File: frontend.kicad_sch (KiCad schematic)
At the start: 71 parts, among them P3 SMA, Q1 NMOS/PMOS, U12 BGS13SN8, U13 74LVC1G86, U14 BGS13SN8, U24 AP22652, U25 TRF37C73, U40 BGB741L7ESD

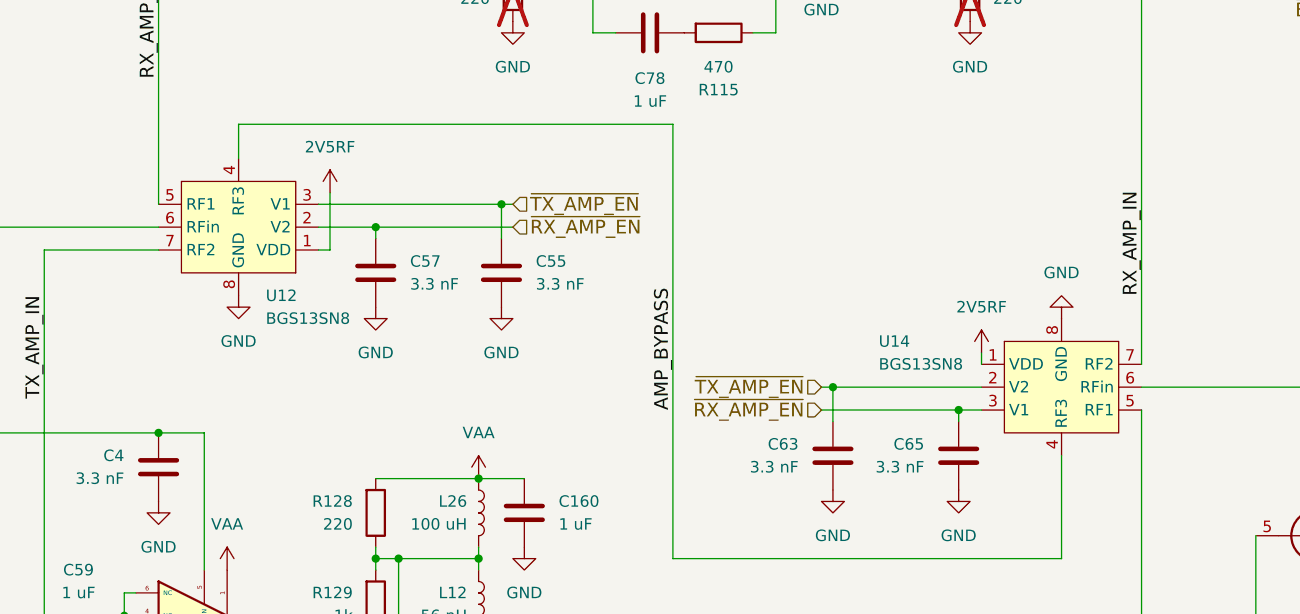
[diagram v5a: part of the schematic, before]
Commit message: Change SP3T RF switches from BGS13SN8 to MXD8638C
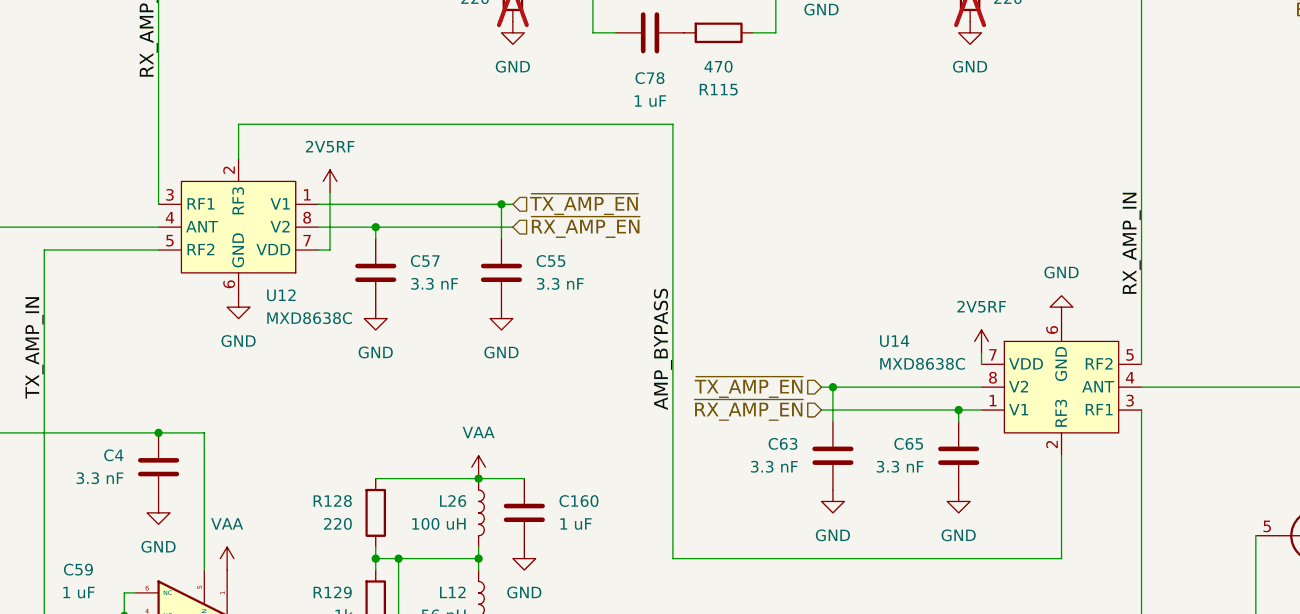
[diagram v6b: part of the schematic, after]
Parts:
- U12, U14: value BGS13SN8 -> MXD8638C; footprint praline:TSNP-9-3 -> praline:MXD8638C; symbol praline:BGS13SN8 -> praline:MXD8638; Manufacturer Infineon -> Maxscend; Part Number BGS13SN8E6327XTSA1 -> MXD8638C
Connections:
- net 2V5RF: now also U12.7 (VDD), U14.7 (VDD); no longer U12.1 (VDD), U14.1 (VDD)
- net AMP_BYPASS: now also U12.2 (RF3), U14.2 (RF3); no longer U12.4 (RF3), U14.4 (RF3)
- net GND: now also U12.6 (GND), U14.6 (GND); no longer U12.8 (GND), U14.8 (GND)
- net RF: now also U12.4 (ANT); no longer U12.6 (RFin)
- net RX_AMP_IN: now also U14.5 (RF2); no longer U14.7 (RF2)
- net RX_AMP_OUT: now also U12.3 (RF1); no longer U12.5 (RF1)
- net TX_AMP_IN: now also U12.5 (RF2); no longer U12.7 (RF2)
- net TX_AMP_OUT: now also U14.3 (RF1); no longer U14.5 (RF1)
- net ~{RX_AMP_EN}: now also U12.8 (V2), U14.1 (V1); no longer U12.2 (V2), U14.3 (V1)
- net ~{TX_AMP_EN}: now also U12.1 (V1), U14.8 (V2); no longer U12.3 (V1), U14.2 (V2)
- net at C68.1: now also U14.4 (ANT); no longer U14.6 (RFin)
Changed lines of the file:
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@@
 	)
 	(symbol
-		(lib_id "praline:BGS13SN8")
+		(lib_id "praline:MXD8638")
 		(at 85.09 97.79 180)
 		(unit 1)
@@
 			)
 		)
-		(property "Value" "BGS13SN8"
+		(property "Value" "MXD8638C"
 			(at 88.1065 107.95 0)
 			(effects
@@
 			)
 		)
-		(property "Footprint" "praline:TSNP-9-3"
+		(property "Footprint" "praline:MXD8638C"
 			(at 85.09 97.79 0)
 			(effects
@@
 			)
 		)
-		(property "Datasheet" "https://www.infineon.com/dgdl/Infineon-BGS13SN8-DS-v02_02-EN.pdf?fileId=5546d462584d1d4a0158cf52e3ae03a7"
+		(property "Datasheet" "~"
 			(at 85.09 97.79 0)
 			(effects
@@
 			)
 		)
-		(property "Manufacturer" "Infineon"
+		(property "Manufacturer" "Maxscend"
 			(at 85.09 97.79 0)
 			(effects
@@
 			)
 		)
-		(property "Part Number" "BGS13SN8E6327XTSA1"
+		(property "Part Number" "MXD8638C"
 			(at 85.09 97.79 0)
 			(effects
@@
 	)
 	(symbol
-		(lib_id "praline:BGS13SN8")
+		(lib_id "praline:MXD8638")
 		(at 176.53 115.57 0)
 		(unit 1)
@@
 			)
 		)
-		(property "Value" "BGS13SN8"
+		(property "Value" "MXD8638C"
 			(at 156.21 113.03 0)
 			(effects
@@
 			)
 		)
-		(property "Footprint" "praline:TSNP-9-3"
+		(property "Footprint" "praline:MXD8638C"
 			(at 176.53 115.57 0)
 			(effects
@@
 			)
 		)
-		(property "Datasheet" "https://www.infineon.com/dgdl/Infineon-BGS13SN8-DS-v02_02-EN.pdf?fileId=5546d462584d1d4a0158cf52e3ae03a7"
+		(property "Datasheet" "~"
 			(at 176.53 115.57 0)
 			(effects
@@
 			)
 		)
-		(property "Manufacturer" "Infineon"
+		(property "Manufacturer" "Maxscend"
 			(at 176.53 115.57 0)
 			(effects
@@
 			)
 		)
-		(property "Part Number" "BGS13SN8E6327XTSA1"
+		(property "Part Number" "MXD8638C"
 			(at 176.53 115.57 0)
 			(effects

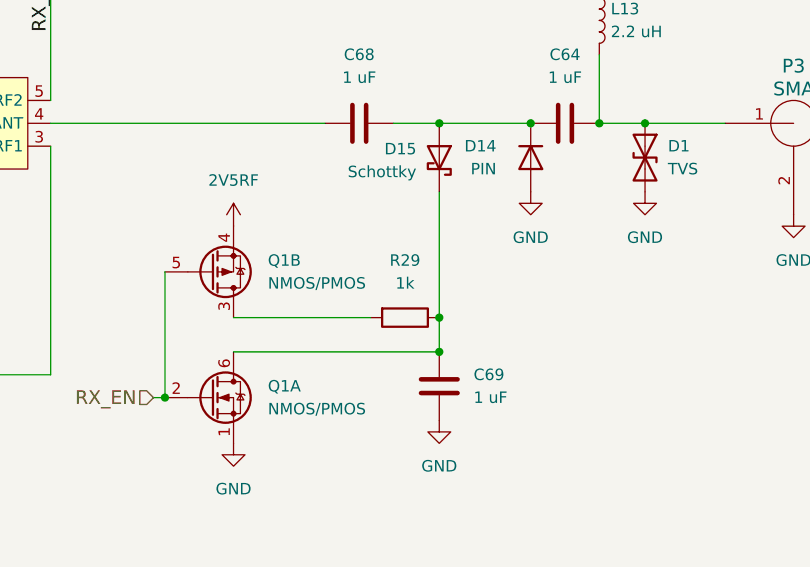
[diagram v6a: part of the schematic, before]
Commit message: Update component selections
- Change C143, C147 to 22 uF CL21A226MAYNNNE
- Change VIN diode D13 to 0 ohm resistor
- Change R29 to 100 ohm
- Change limiter Schottky D15 to JDH2S02SL,L3F
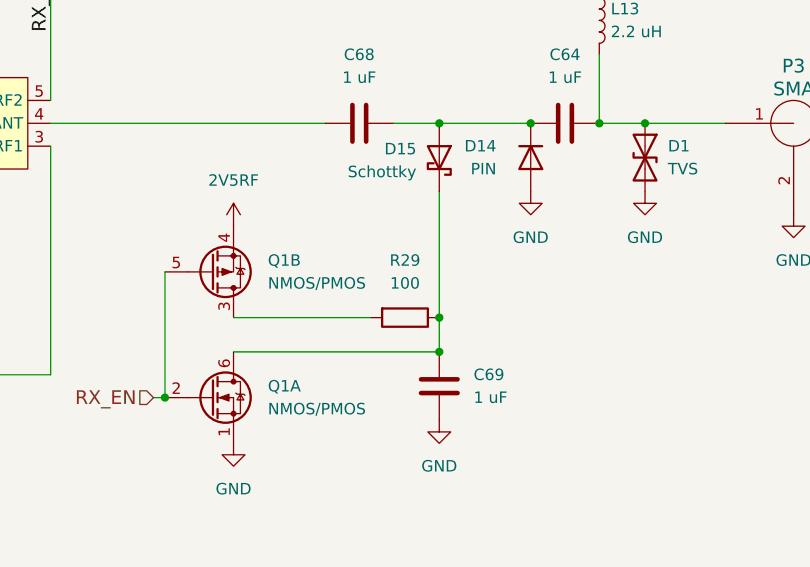
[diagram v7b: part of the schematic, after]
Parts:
- D15: Manufacturer Infineon -> Toshiba; Part Number BAT1502LSE6327XTSA1 -> JDH2S02SL,L3F; Substitution BAT1502LSE6433XTMA1, BAT1502ELSE6327XTSA1, BAT2402LSE6327XT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 -> (none)
- R29: value 1k -> 100; Part Number RC0201FR-071KL -> RC0201JR-07100RL
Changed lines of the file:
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@@
 			)
 		)
-		(property "Value" "1k"
+		(property "Value" "100"
 			(at 224.79 133.35 90)
 			(effects
@@
 			)
 		)
-		(property "Description" "RES 1K OHM 1% 1/20W 0201"
+		(property "Description" "RES 100 OHM 5% 1/20W 0201"
 			(at 224.79 137.16 0)
 			(effects
@@
 			)
 		)
-		(property "Part Number" "RC0201FR-071KL"
+		(property "Part Number" "RC0201JR-07100RL"
 			(at 224.79 137.16 0)
 			(effects
@@
 			)
 		)
-		(property "Datasheet" "~"
+		(property "Datasheet" "https://www.lcsc.com/datasheet/C285557.pdf"
 			(at 85.09 97.79 0)
 			(effects
@@
 			)
 		)
-		(property "Datasheet" "~"
+		(property "Datasheet" "https://assets.nexperia.com/documents/data-sheet/PMEG4010ESB.pdf"
 			(at 265.43 66.04 0)
 			(effects
@@
 			)
 		)
-		(property "Datasheet" "~"
+		(property "Datasheet" "https://www.infineon.com/dgdl/Infineon-BAR90-02EL-DS-v01_00-EN.pdf?fileId=5546d46265f064ff01663895cd694e6e"
 			(at 238.76 119.38 0)
 			(effects
@@
 			)
 		)
-		(property "Datasheet" "~"
+		(property "Datasheet" "https://toshiba.semicon-storage.com/info/docget.jsp?did=30457&prodName=JDH2S02SL"
 			(at 228.6 119.38 0)
 			(effects
@@
 			)
 		)
-		(property "Description" "DIODE SCHOTTKY 4V 100MW TSSLP23"
+		(property "Description" "DIODE SCHOTTKY 10V 10MA SL2"
 			(at 228.6 119.38 0)
 			(effects
@@
 			)
 		)
-		(property "Manufacturer" "Infineon"
+		(property "Manufacturer" "Toshiba"
 			(at 228.6 119.38 90)
 			(effects
@@
 			)
 		)
-		(property "Part Number" "BAT1502LSE6327XTSA1"
+		(property "Part Number" "JDH2S02SL,L3F"
 			(at 228.6 119.38 90)
 			(effects
@@
 			)
 		)
-		(property "Substitution" "BAT1502LSE6433XTMA1, BAT1502ELSE6327XTSA1, BAT2402LSE6327XTSA1, BAT2402ELSE6327XTSA1"
+		(property "Substitution" ""
 			(at 228.6 119.38 90)
 			(effects
@@
 			)
 		)
-		(property "Datasheet" "~"
+		(property "Datasheet" "https://www.lcsc.com/datasheet/C285557.pdf"
 			(at 176.53 115.57 0)
 			(effects
